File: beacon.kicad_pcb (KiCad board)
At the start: 2 copper layers, 45 x 30 mm, 60 parts, among them SW1 RST, U1 NUF2042XV6, U2 SN65HVD256, U3 MPU-9250, U4 LT1965-3.3, U5 STM32F405RGT6, U6 DWM1000, X1 16MHz

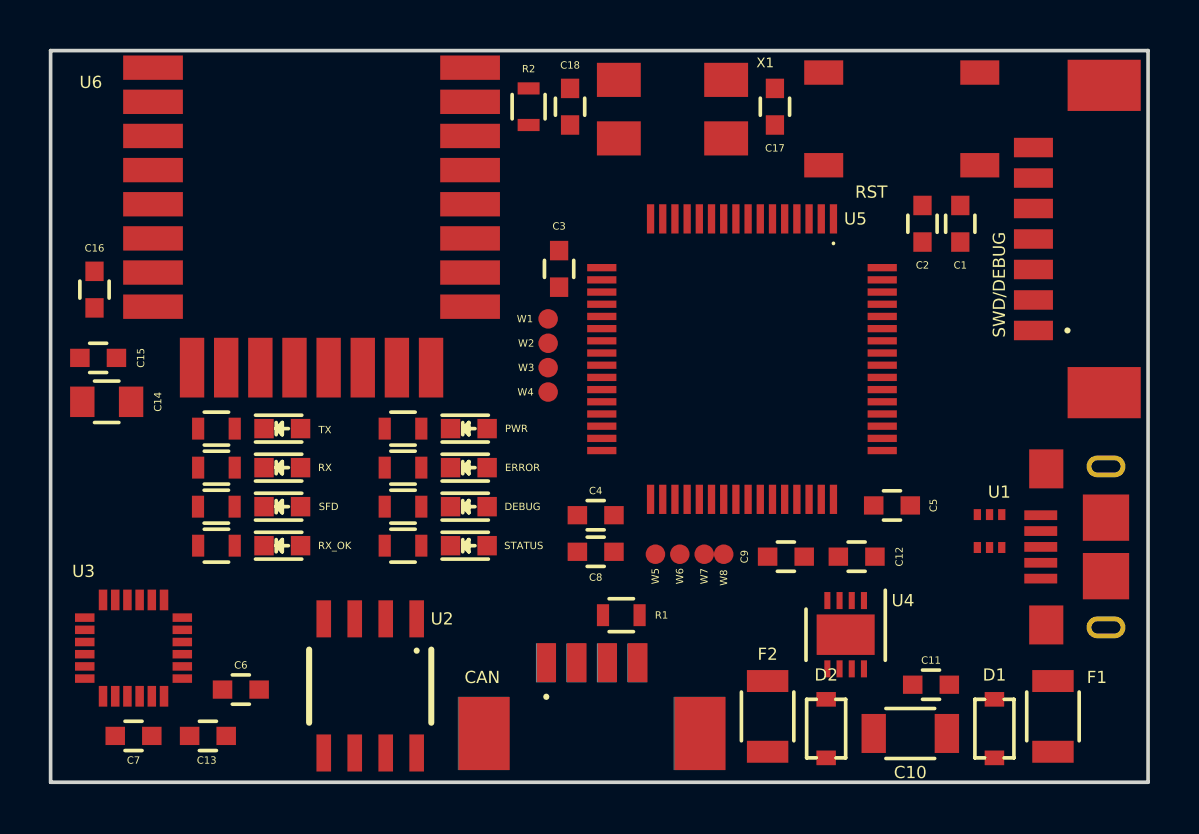
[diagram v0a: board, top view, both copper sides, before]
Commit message: Update component placement
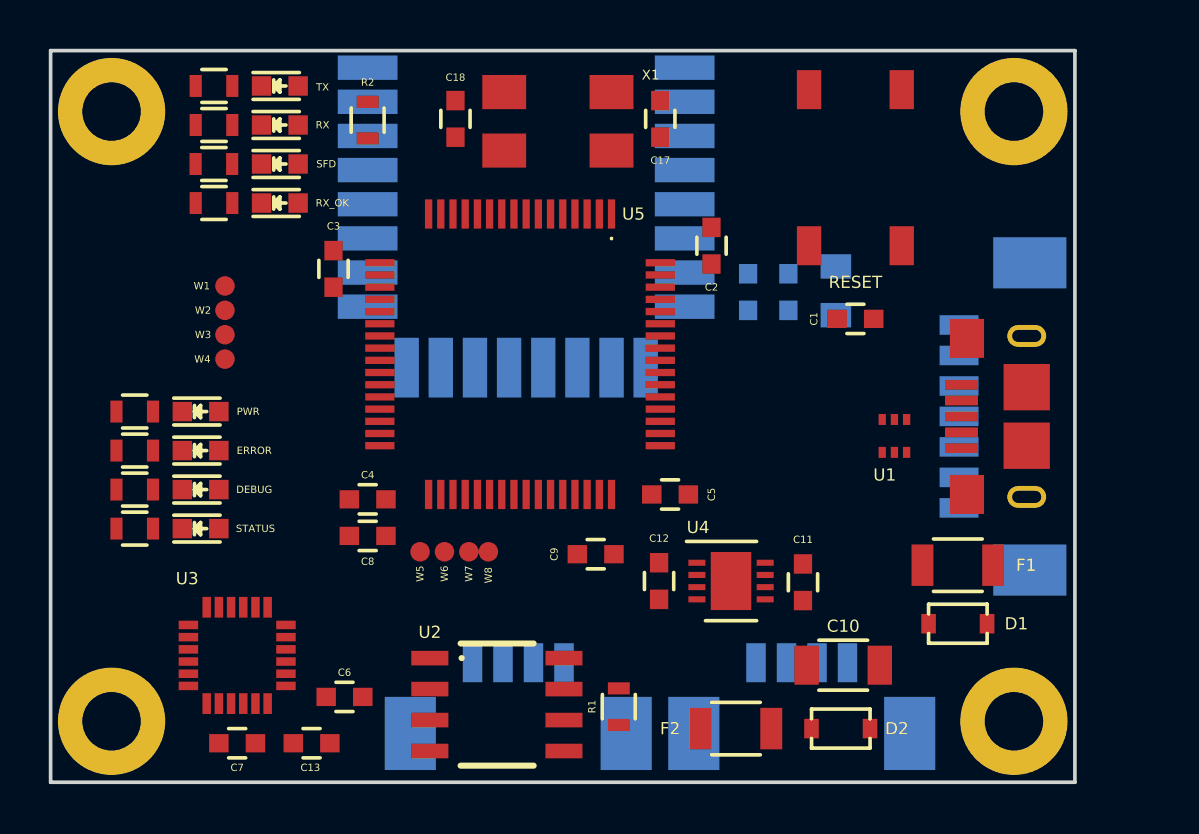
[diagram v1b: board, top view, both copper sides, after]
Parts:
- added _M2: VAL**, _mech:_M2, F.Cu at (117.5, 62.5)
- added _M2: VAL**, _mech:_M2, F.Cu at (154.5, 87.5)
- added _M2: VAL**, _mech:_M2, F.Cu at (117.5, 87.5)
- added _M2: VAL**, _mech:_M2, F.Cu at (154.5, 62.5)
- C14, C15, C16, CONN2, CONN4, U6: moved to B.Cu
- SW1: value RST -> RESET
- moved C14 30.2 mm to (147.2, 69.8), turned to 270 degrees
- moved C15 28.4 mm to (145.2, 69.9), turned to 270 degrees
- moved C16 26.8 mm to (143.6, 69.9)
- moved U6 21.8 mm to (141.0, 60.7), turned to 180 degrees
- moved D10 14.1 mm to (124.4, 66.2)
- moved D7 14.1 mm to (124.4, 61.5)
- moved D8 14.1 mm to (124.4, 63.0)
- moved D9 14.1 mm to (124.4, 64.7)
- moved R10 14.1 mm to (121.7, 66.2)
- moved R7 14.1 mm to (121.7, 61.5)
- moved R8 14.1 mm to (121.7, 63.0)
- moved R9 14.1 mm to (121.7, 64.7)
- moved W1 13.3 mm to (122.2, 69.7)
- moved W2 13.3 mm to (122.2, 70.7)
- moved W3 13.3 mm to (122.2, 71.7)
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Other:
- board size 45 x 30 mm -> 42 x 30 mm

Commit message: Add mounting holes and fix testpads
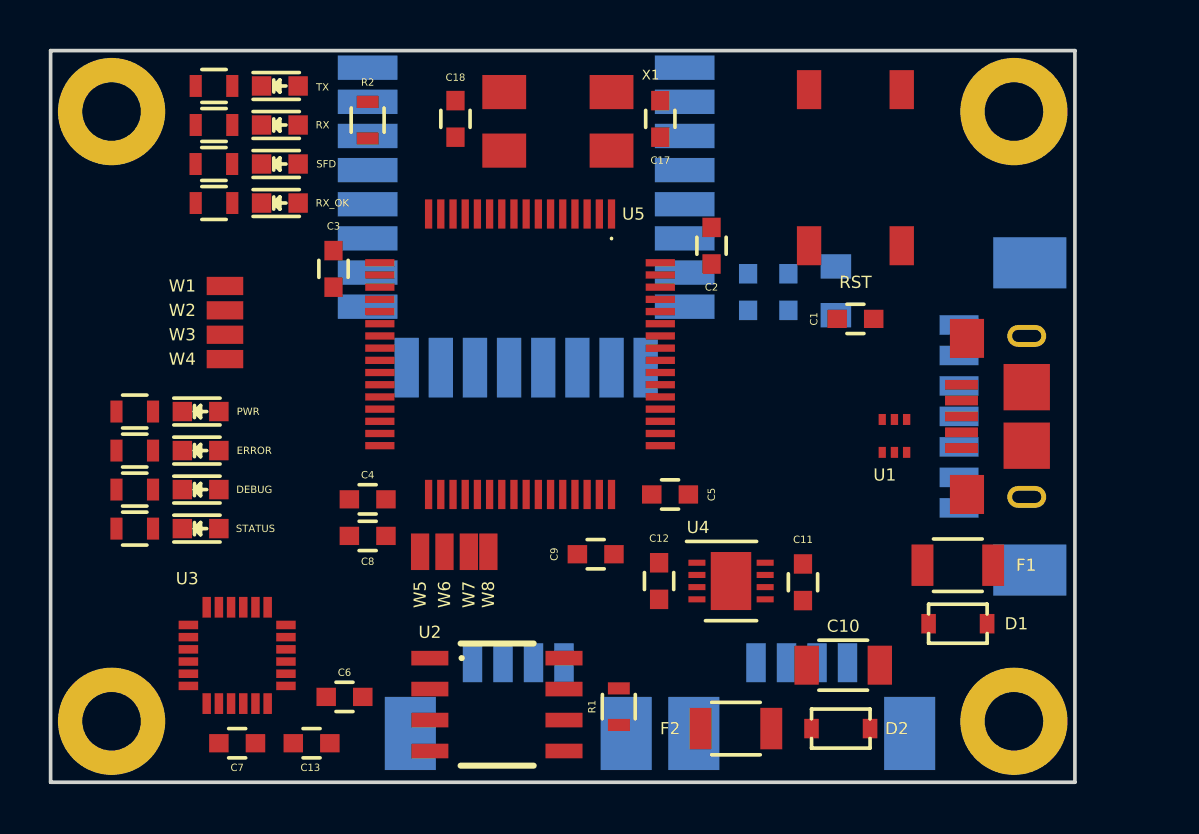
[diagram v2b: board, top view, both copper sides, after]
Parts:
- removed _M2 (x4): VAL**, _mech:_M2
- added H1: M2_HOLE, _mech:_M2, F.Cu at (117.5, 87.5)
- added H2: M2_HOLE, _mech:_M2, F.Cu at (154.5, 62.5)
- added H3: M2_HOLE, _mech:_M2, F.Cu at (117.5, 62.5)
- added H4: M2_HOLE, _mech:_M2, F.Cu at (154.5, 87.5)
- SW1: value RESET -> RST
- W1, W2, W3, W5: footprint _std:Measurement_Point_Round-SMD-Pad_Small -> _div:Test_1pin_SMD
- W4: value TEST_UWB_MOSi -> TEST_UWB_MOSI; footprint _std:Measurement_Point_Round-SMD-Pad_Small -> _div:Test_1pin_SMD
- W6: value TEST_IMU_CLK -> TEST_UWB_SCK; footprint _std:Measurement_Point_Round-SMD-Pad_Small -> _div:Test_1pin_SMD
- W7: value TEST_IMU_MISO -> TEST_UWB_MISO; footprint _std:Measurement_Point_Round-SMD-Pad_Small -> _div:Test_1pin_SMD
- W8: value TEST_IMU_MOSi -> TEST_UWB_MOSI; footprint _std:Measurement_Point_Round-SMD-Pad_Small -> _div:Test_1pin_SMD
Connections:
- U5 pad 20: Net-(U5-Pad20) -> /UWB_CS_N
- U5 pad 21: Net-(U5-Pad21) -> /UWB_CLK
- U5 pad 22: Net-(U5-Pad22) -> /UWB_MISO
- U5 pad 23: Net-(U5-Pad23) -> /UWB_MOSI
- U5 pad 33: Net-(U5-Pad33) -> /IMU_CS_N
- U5 pad 34: Net-(U5-Pad34) -> /IMU_SCK
- U5 pad 35: Net-(U5-Pad35) -> /IMU_MISO
- U5 pad 36: Net-(U5-Pad36) -> /IMU_MOSI
- W1 pad 1: Net-(U5-Pad20) -> /UWB_CS_N
- W2 pad 1: Net-(U5-Pad21) -> /UWB_CLK
- W3 pad 1: Net-(U5-Pad22) -> /UWB_MISO
- W4 pad 1: Net-(U5-Pad23) -> /UWB_MOSI
- W5 pad 1: Net-(U5-Pad33) -> /IMU_CS_N
- W6 pad 1: Net-(U5-Pad34) -> /IMU_SCK
- W7 pad 1: Net-(U5-Pad35) -> /IMU_MISO
- W8 pad 1: Net-(U5-Pad36) -> /IMU_MOSI

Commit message: Add logo
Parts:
- added G***: LOGO, _logo:CVRA-logo-big, B.Cu at (121.4, 72.4)
- added G***: LOGO, _logo:CVRA-logo-small, F.Cu at (153.9, 67.8)
- D10: value RX_OK -> RXOK
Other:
- board text added: "UWB Beacon board v1.0 Club Vaudois de Robotique Autonome cvra.ch"

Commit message: Route PCB
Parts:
- moved C9 1.55 mm to (135.8, 80.7), turned to 180 degrees
- moved C7 0.65 mm to (122.0, 88.4)
- moved W7 0.10 mm to (132.1, 80.5)
- moved W6 0.05 mm to (131.1, 80.5)
- moved W8 0.05 mm to (133.0, 80.5)
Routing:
- net VCC: track 0.00 -> 161.5 mm, vias 0 -> 1
- net GND: track 0.00 -> 115.3 mm, vias 0 -> 14
- net /UWB_RST_N: track 0.00 -> 47.1 mm, vias 0 -> 1
- net +5V_protected: track 0.00 -> 46.8 mm
- net /UART_RX: track 0.00 -> 39.3 mm, vias 0 -> 1
- net /UWB_IRQ: track 0.00 -> 39.2 mm, vias 0 -> 2
- net /STM32_NRST: track 0.00 -> 36.0 mm, vias 0 -> 4
- net /UART_TX: track 0.00 -> 35.9 mm, vias 0 -> 1
- net /CAN1_SILENT: track 0.00 -> 25.6 mm, vias 0 -> 2
- net /CAN1_RX: track 0.00 -> 24.9 mm, vias 0 -> 2
- net /UWB_CS_N: track 0.00 -> 23.8 mm, vias 0 -> 1
- net /CAN1_TX: track 0.00 -> 23.6 mm, vias 0 -> 2
- net /IMU_INT: track 0.00 -> 22.9 mm, vias 0 -> 2
- net Net-(CONN2-Pad3): track 0.00 -> 20.8 mm, vias 0 -> 2
- net /IMU_MISO: track 0.00 -> 20.5 mm, vias 0 -> 2
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- added copper zone on B.Cu, net GND
- added copper zone on F.Cu, net GND
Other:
- net class Default: trace_width 0.25 -> 0.2
- rule trace_min: 0.2 -> 0.15

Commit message: Generate gerber files
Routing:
- net VCC: track 161.5 -> 167.7 mm

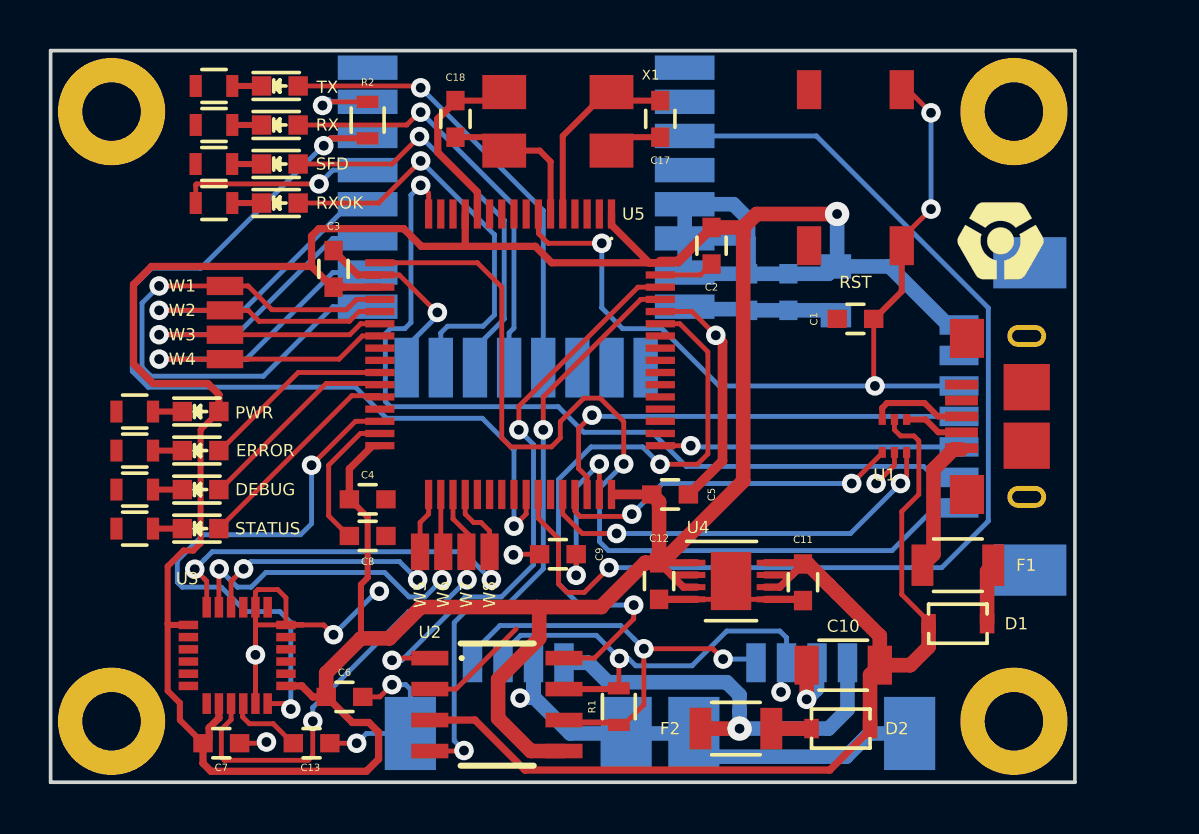
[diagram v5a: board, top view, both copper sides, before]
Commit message: Correct PCB routing from review remarks
- MPU9250 footprint
- Missing vias for good ground
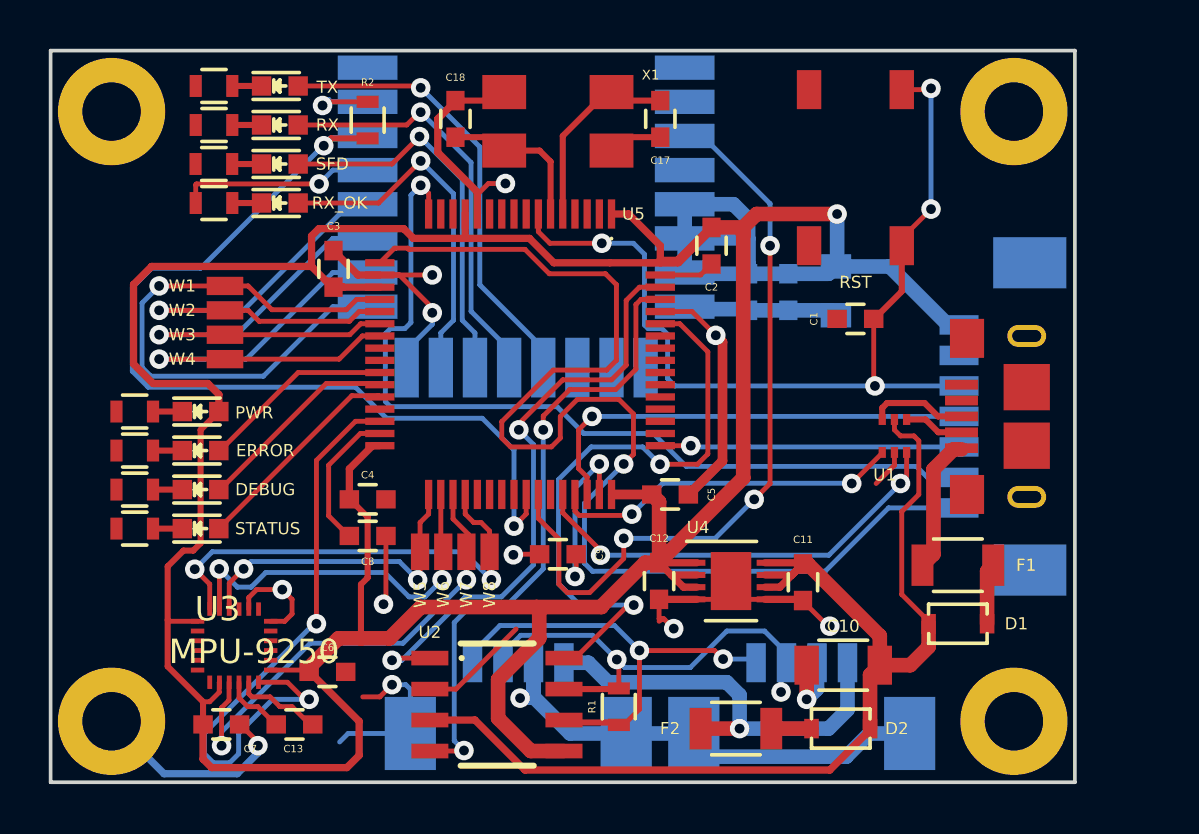
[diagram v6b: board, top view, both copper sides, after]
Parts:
- removed G***: LOGO, _logo:CVRA-logo-big
- removed G***: LOGO, _logo:CVRA-logo-small
- D10: value RXOK -> RX_OK
- moved C6 1.24 mm to (126.3, 85.5)
- moved C13 1.04 mm to (125.0, 87.6)
- moved C7 0.77 mm to (122.0, 87.6)
- moved U3 0.42 mm to (122.5, 84.4)
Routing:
- net /UWB_RST_N: track 47.1 -> 32.1 mm, vias 1 -> 3
- net /UART_RX: track 39.3 -> 50.7 mm
- net GND: track 115.3 -> 120.7 mm, vias 14 -> 15
- net /IMU_INT: track 22.9 -> 25.6 mm
- net /UWB_RX_OK: track 17.2 -> 15.0 mm
- net /STM32_NRST: track 36.0 -> 37.8 mm
- net VCC: track 167.7 -> 166.4 mm
- net /CAN1_TX: track 23.6 -> 24.7 mm
- net /CAN1_RX: track 24.9 -> 26.0 mm
- net /UWB_SFD: track 16.9 -> 15.9 mm
- net /USB_DM: track 17.2 -> 18.0 mm
- net /IMU_MISO: track 20.5 -> 19.7 mm
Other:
- net class Default: clearance 0.2 -> 0.16
- rule trace_clearance: 0.2 -> 0.16

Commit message: Corrections from review remarks
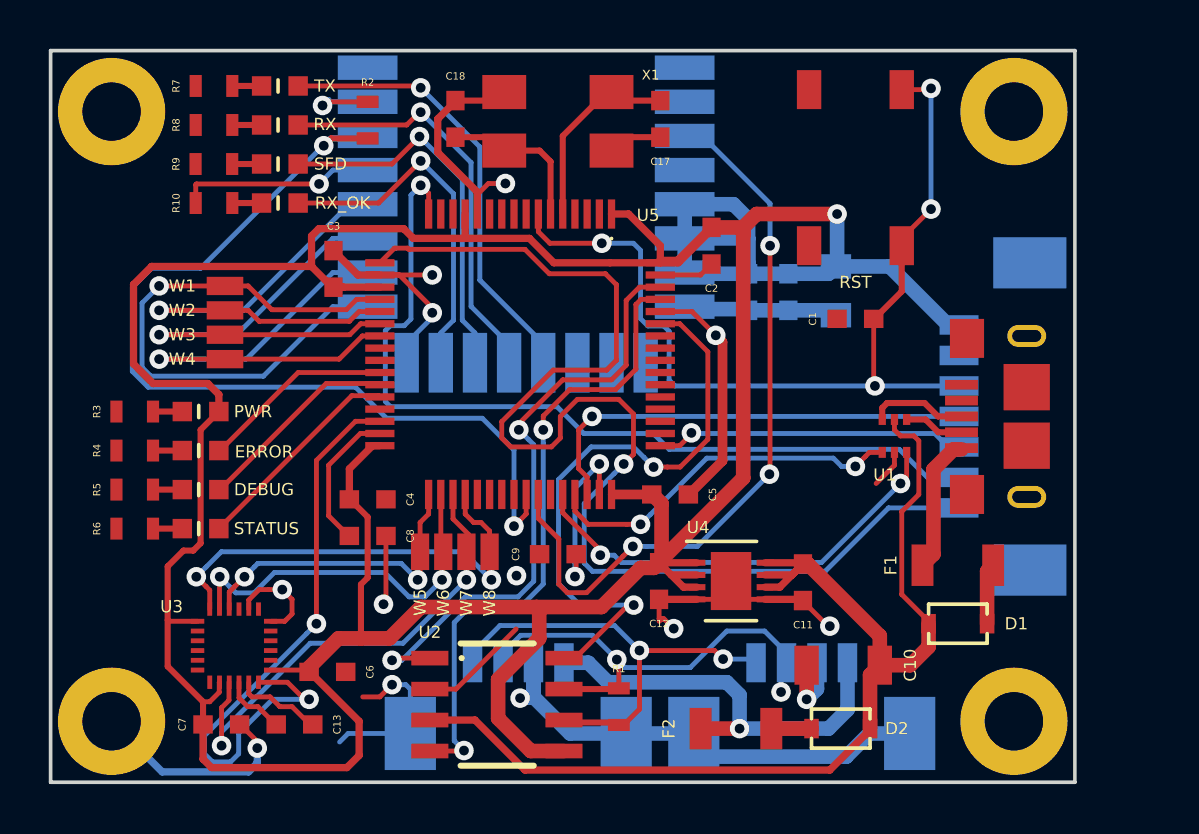
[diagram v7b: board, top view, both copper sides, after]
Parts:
- C1, C11, C12, C13, C15, C16, C17, C18, C2, C3, C4, C5, C6, C7, C8, C9: footprint Capacitors_SMD:C_0603 -> _std:C_0603
- C10: footprint Capacitors_SMD:C_1206 -> _std:C_1206
- C14: footprint Capacitors_SMD:C_0805 -> _std:C_0805
- D10, D3, D4, D5, D6, D7, D8, D9: footprint _std:_LED_0603 -> _std:D_0603
- F1, F2: footprint Resistors_SMD:R_1206 -> _std:R_1206
- R1, R10, R2, R3, R4, R5, R6, R7, R8, R9: footprint Resistors_SMD:R_0603 -> _std:R_0603
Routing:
- net GND: track 120.7 -> 119.8 mm
- net /UWB_RST_N: track 32.1 -> 31.4 mm
- net /USB_DP: track 14.5 -> 15.0 mm

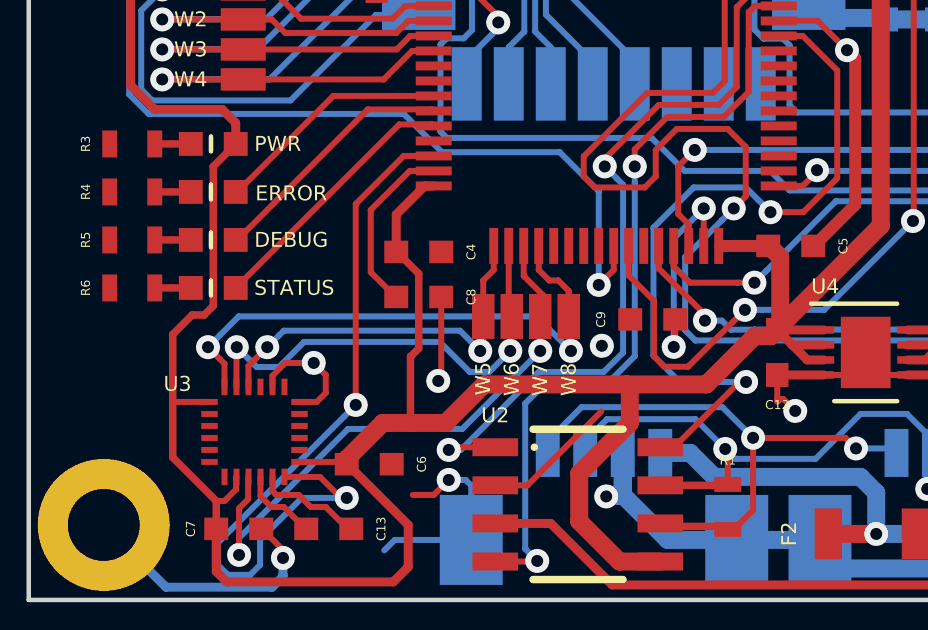
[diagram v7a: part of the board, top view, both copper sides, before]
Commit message: Rewire UWB reset to not interfere with VUSB sense
Fixes #2
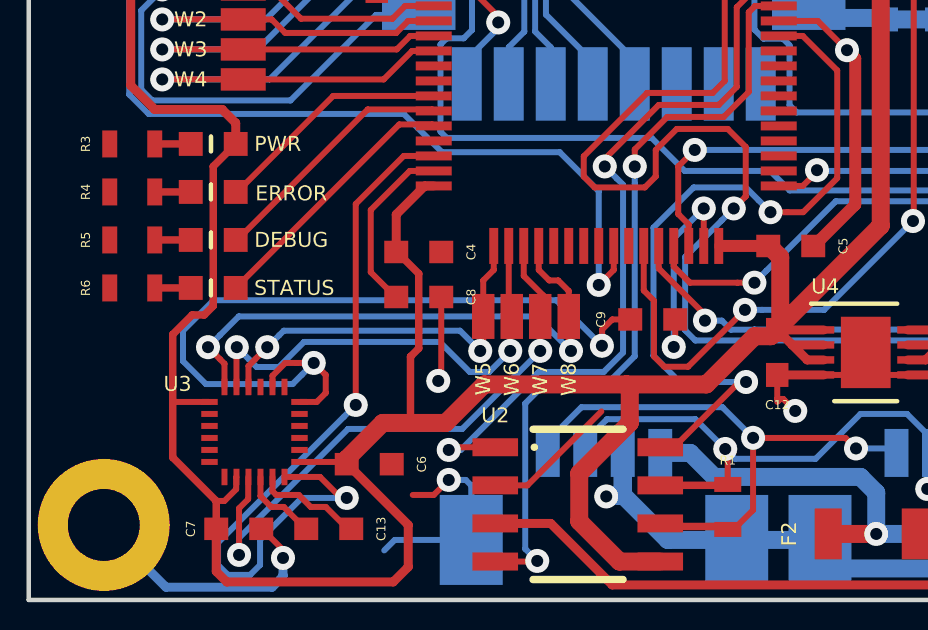
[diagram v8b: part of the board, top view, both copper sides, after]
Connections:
- U5 pad 42: /UWB_RST_N -> Net-(U5-Pad42)
- U5 pad 43: Net-(U5-Pad43) -> /UWB_RST_N
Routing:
- net GND: track 119.8 -> 142.4 mm
